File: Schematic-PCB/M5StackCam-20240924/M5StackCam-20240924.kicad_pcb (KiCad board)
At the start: 2 copper layers, 20.3 x 14.5 mm, 3 parts, among them J1 Conn_CamL, J2 Conn_CamR, J3 Conn_Output

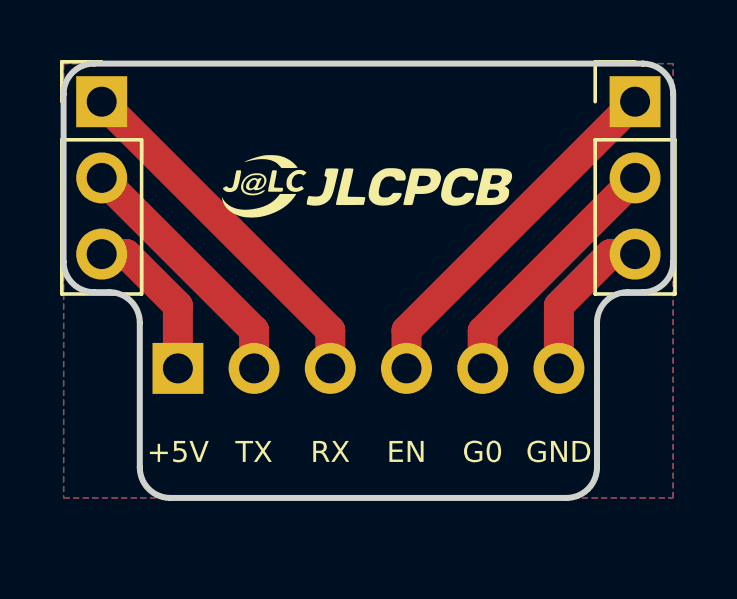
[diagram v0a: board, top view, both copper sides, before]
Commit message: update: カメラ接続用基板の基板外形を更新した
発注用ファイルも同時に出力しておいた
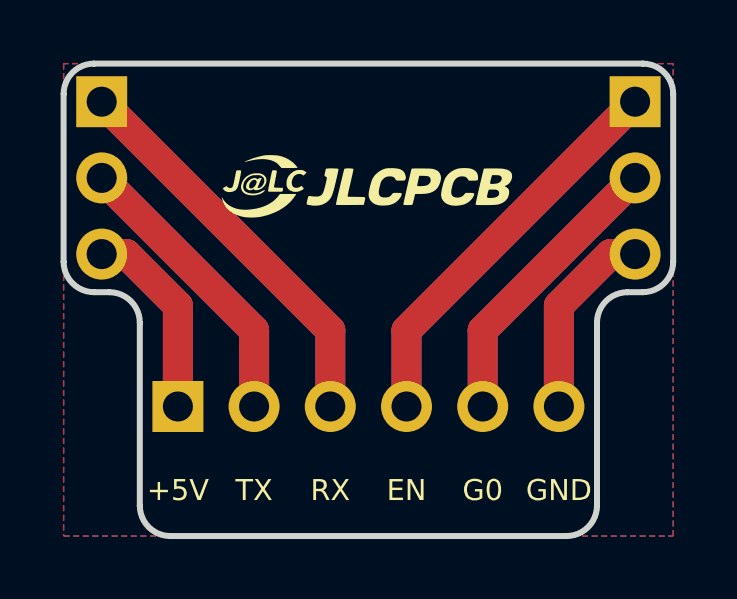
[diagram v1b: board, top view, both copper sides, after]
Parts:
- J1, J2: moved to B.Cu
- moved J3 1.27 mm to (2.54, 7.62)
- turned J1 to 180 degrees
- turned J2 to 180 degrees
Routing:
- net RX: track 12.0 -> 26.6 mm
- net EN: track 12.0 -> 26.6 mm
- net G0: track 8.45 -> 19.4 mm
- net TX: track 8.45 -> 19.4 mm
- net GND: track 5.34 -> 13.2 mm
- net +5V: track 5.34 -> 13.2 mm
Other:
- board size 20.3 x 14.5 mm -> 20.3 x 15.7 mm
